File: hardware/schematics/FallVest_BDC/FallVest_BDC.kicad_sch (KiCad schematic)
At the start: 6 parts, among them U1 STP55NF06L, U2 TO-220, U3 4554

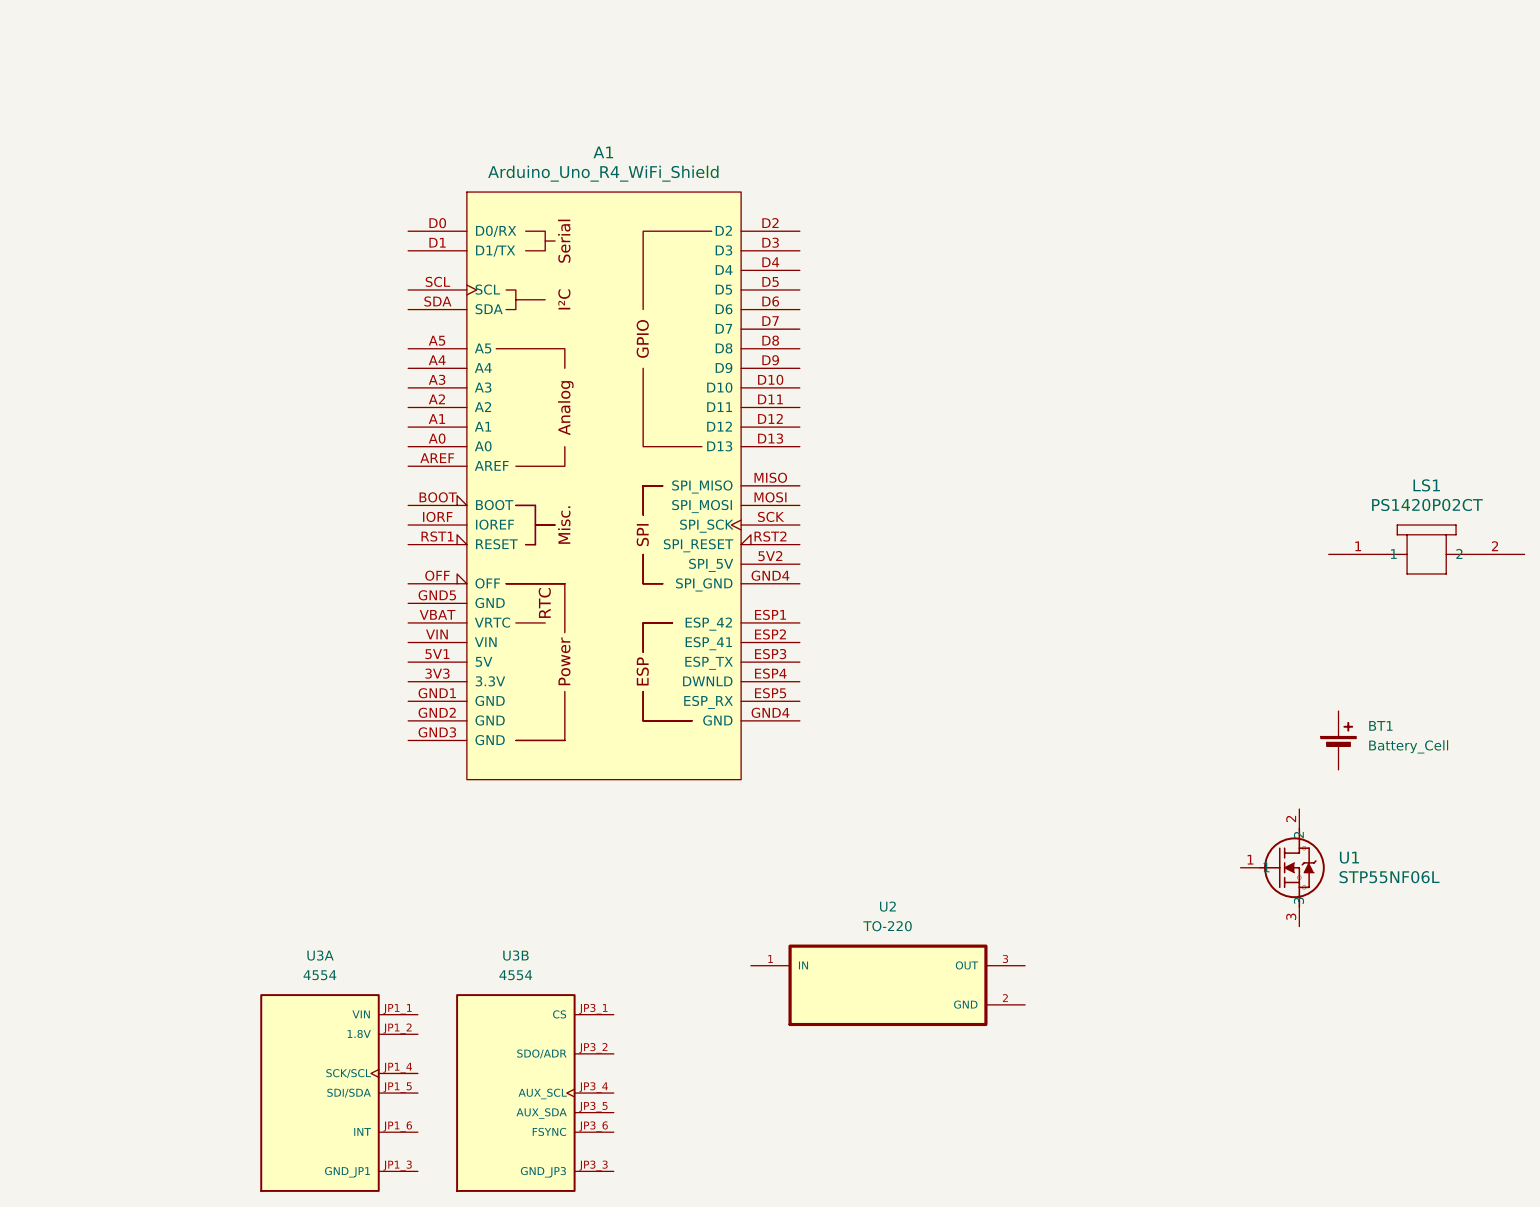
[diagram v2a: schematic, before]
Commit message: Wired most components
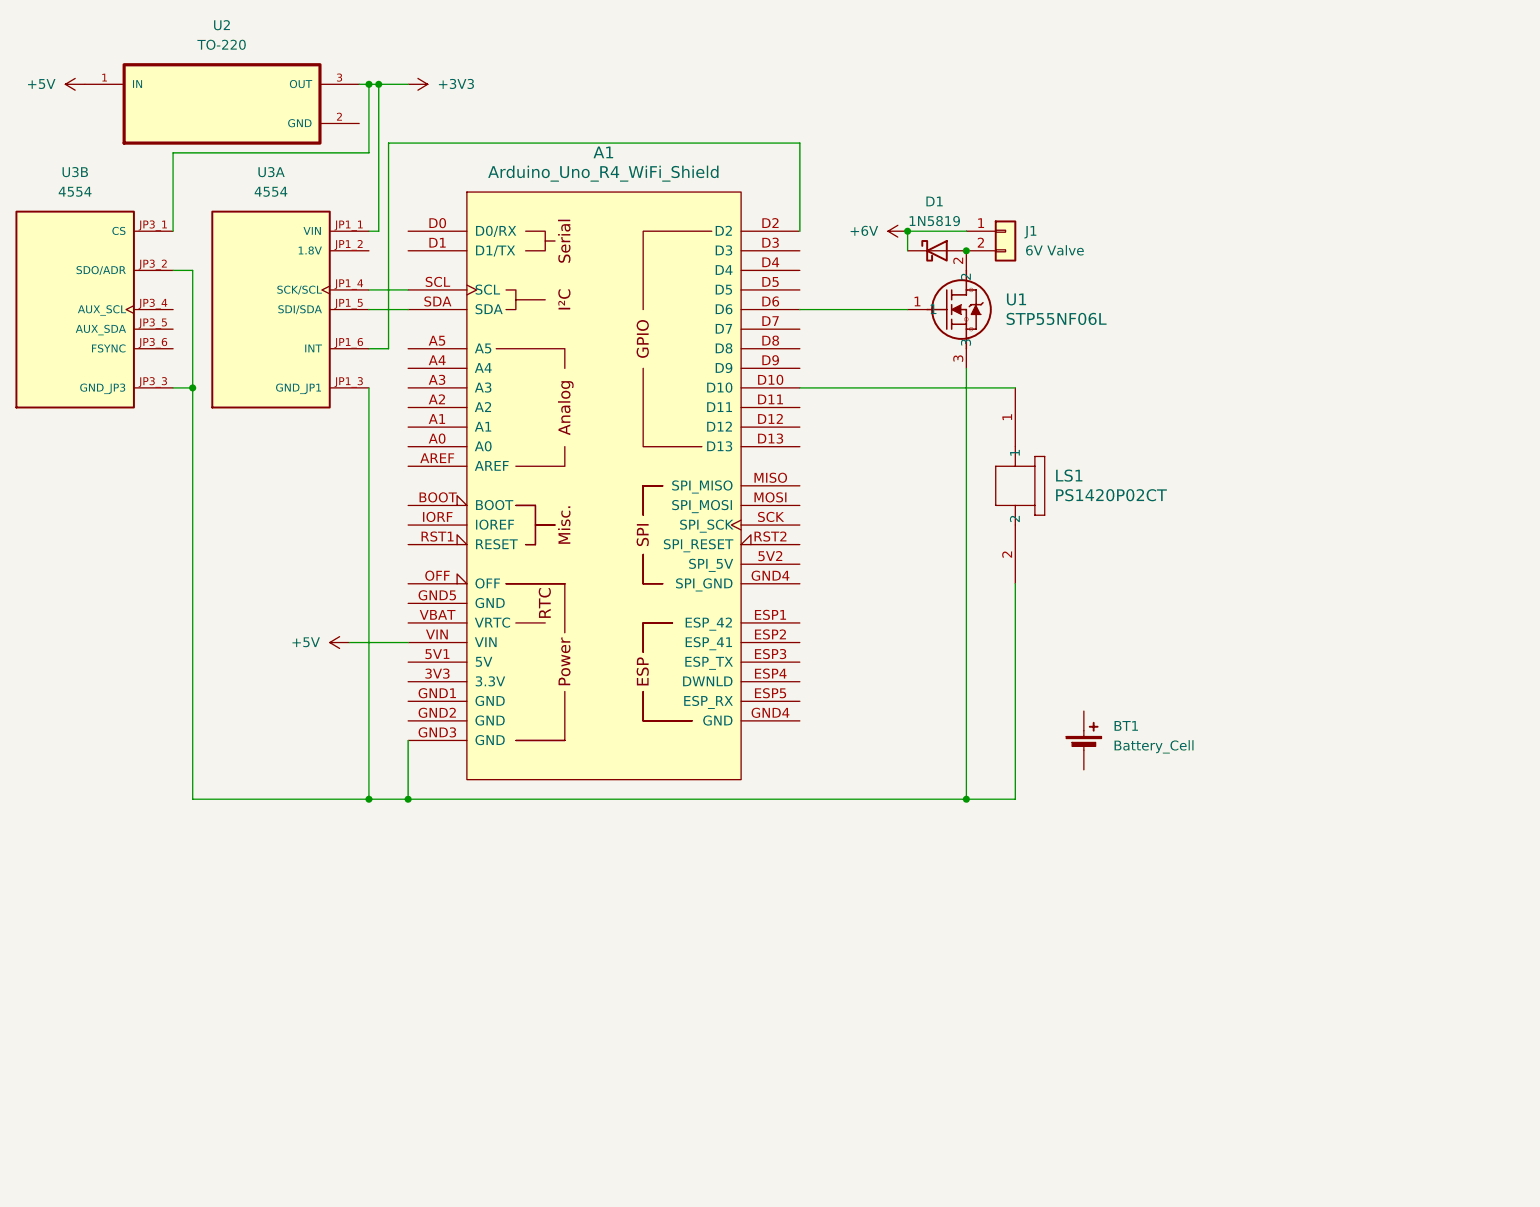
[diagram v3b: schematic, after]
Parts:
- added D1: 1N5819, Diode_THT:D_DO-41_SOD81_P10.16mm_Horizontal, symbol Diode:1N5819
- added J1: 6V Valve, symbol Connector_Generic:Conn_01x02
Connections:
- net +3V3: now reaches U3.JP3_1 (CS)
- net +3V3: now also U2.3 (OUT), U3.JP1_1 (VIN)
- net at U3.JP3_2 (SDO/ADR): now also A1.GND3 (GND), LS1.2, U1.3, U3.JP1_3 (GND_JP1), U3.JP3_3 (GND_JP3)
- net at LS1.1: now also A1.D10
- net at U3.JP1_4 (SCK/SCL): now also A1.SCL
- net at U3.JP1_5 (SDI/SDA): now also A1.SDA
- net at U3.JP1_6 (INT): now also A1.D2
- net at A1.D6: now also U1.1
- net +5V: now reaches A1.VIN
- net +5V: now also U2.1 (IN)
- net at U1.2: now also D1.2 (A), J1.2 (Pin_2)
- new net +6V: D1.1 (K), J1.1 (Pin_1)
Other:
- moved on the sheet: BT1, LS1, U1, U2, U3A, U3B

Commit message: Updated Schematic
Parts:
- removed D1: 1N5819, Diode_THT:D_DO-41_SOD81_P10.16mm_Horizontal, symbol Diode:1N5819
- removed J1: 6V Valve, symbol Connector_Generic:Conn_01x02
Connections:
- net at A1.GND3 (GND), U1.3, U3.JP1_3 (GND_JP1)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: no longer LS1.2
- net at LS1.1: now also A1.5V1 (5V); no longer A1.D10
- net at U1.2: now also LS1.2
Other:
- moved on the sheet: BT1, LS1

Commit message: Moving around and adding some stuff
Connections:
- net GND: now reaches A1.GND3 (GND), U1.3, U3.JP1_3 (GND_JP1), U3.JP3_2 (SDO/ADR), U3.JP3_3 (GND_JP3)
- net GND: now also U2.2 (GND)
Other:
- moved on the sheet: BT1, U2

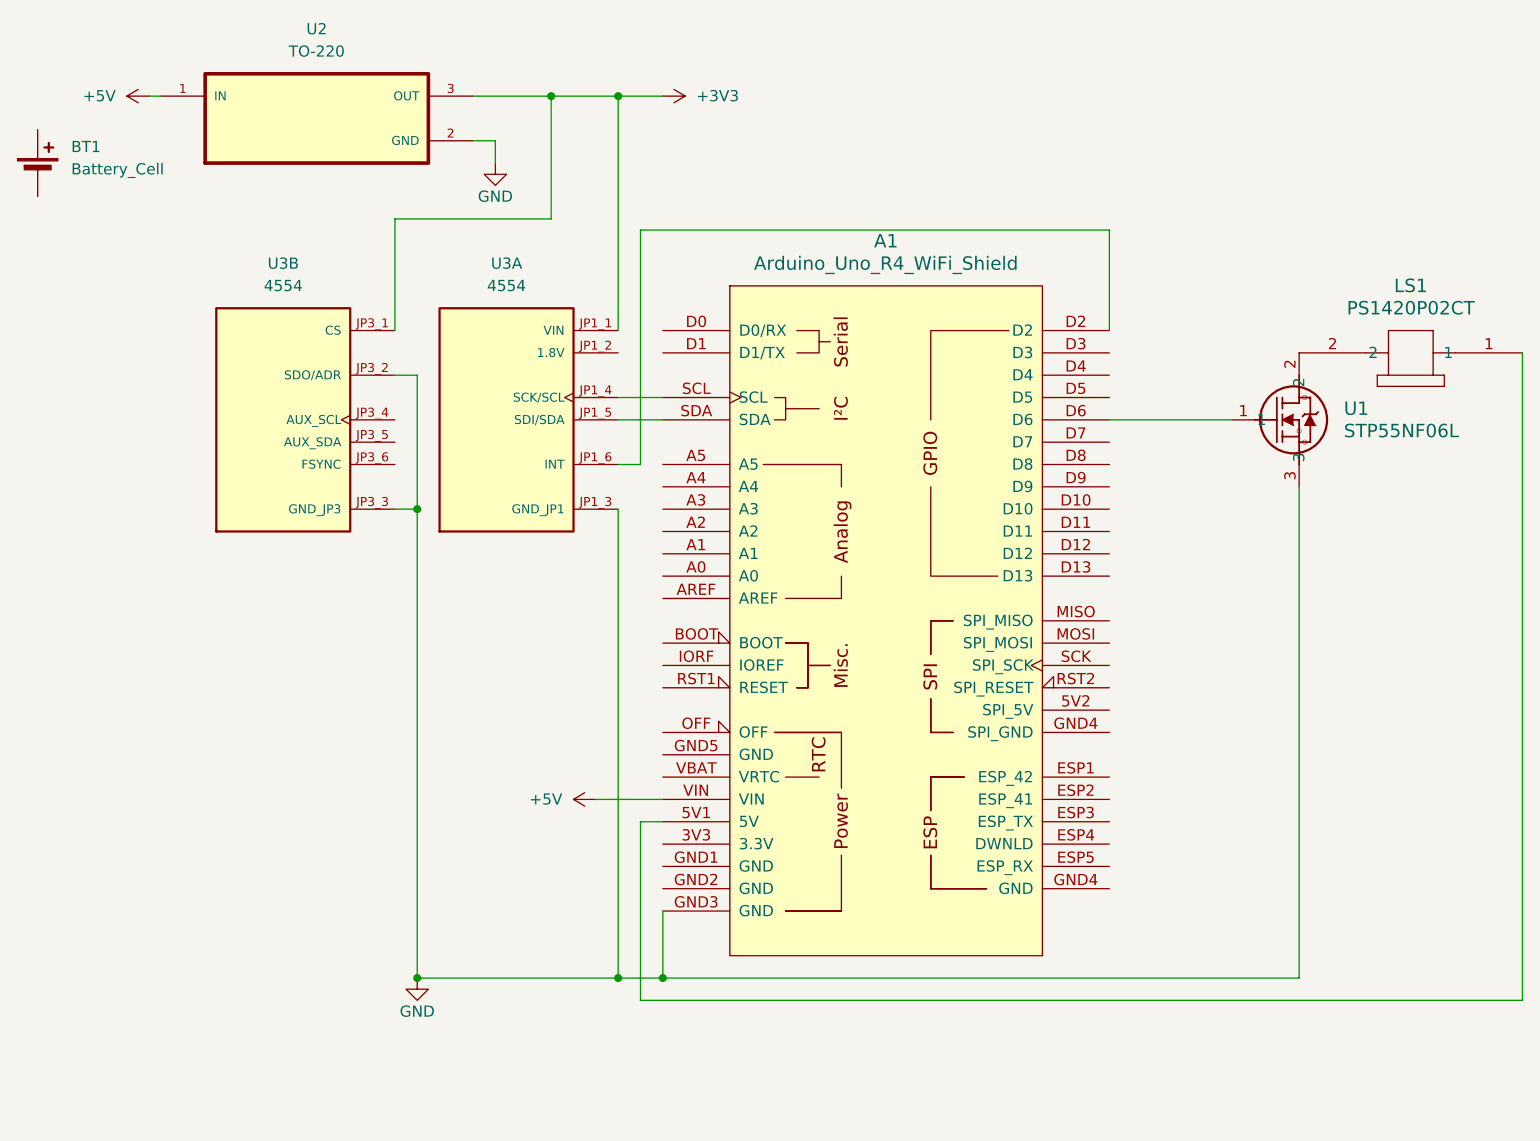
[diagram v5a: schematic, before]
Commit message: Modified
Got rid of the regulator, need to check on pinout for sensor, and where the air valve will be located in the circuit.
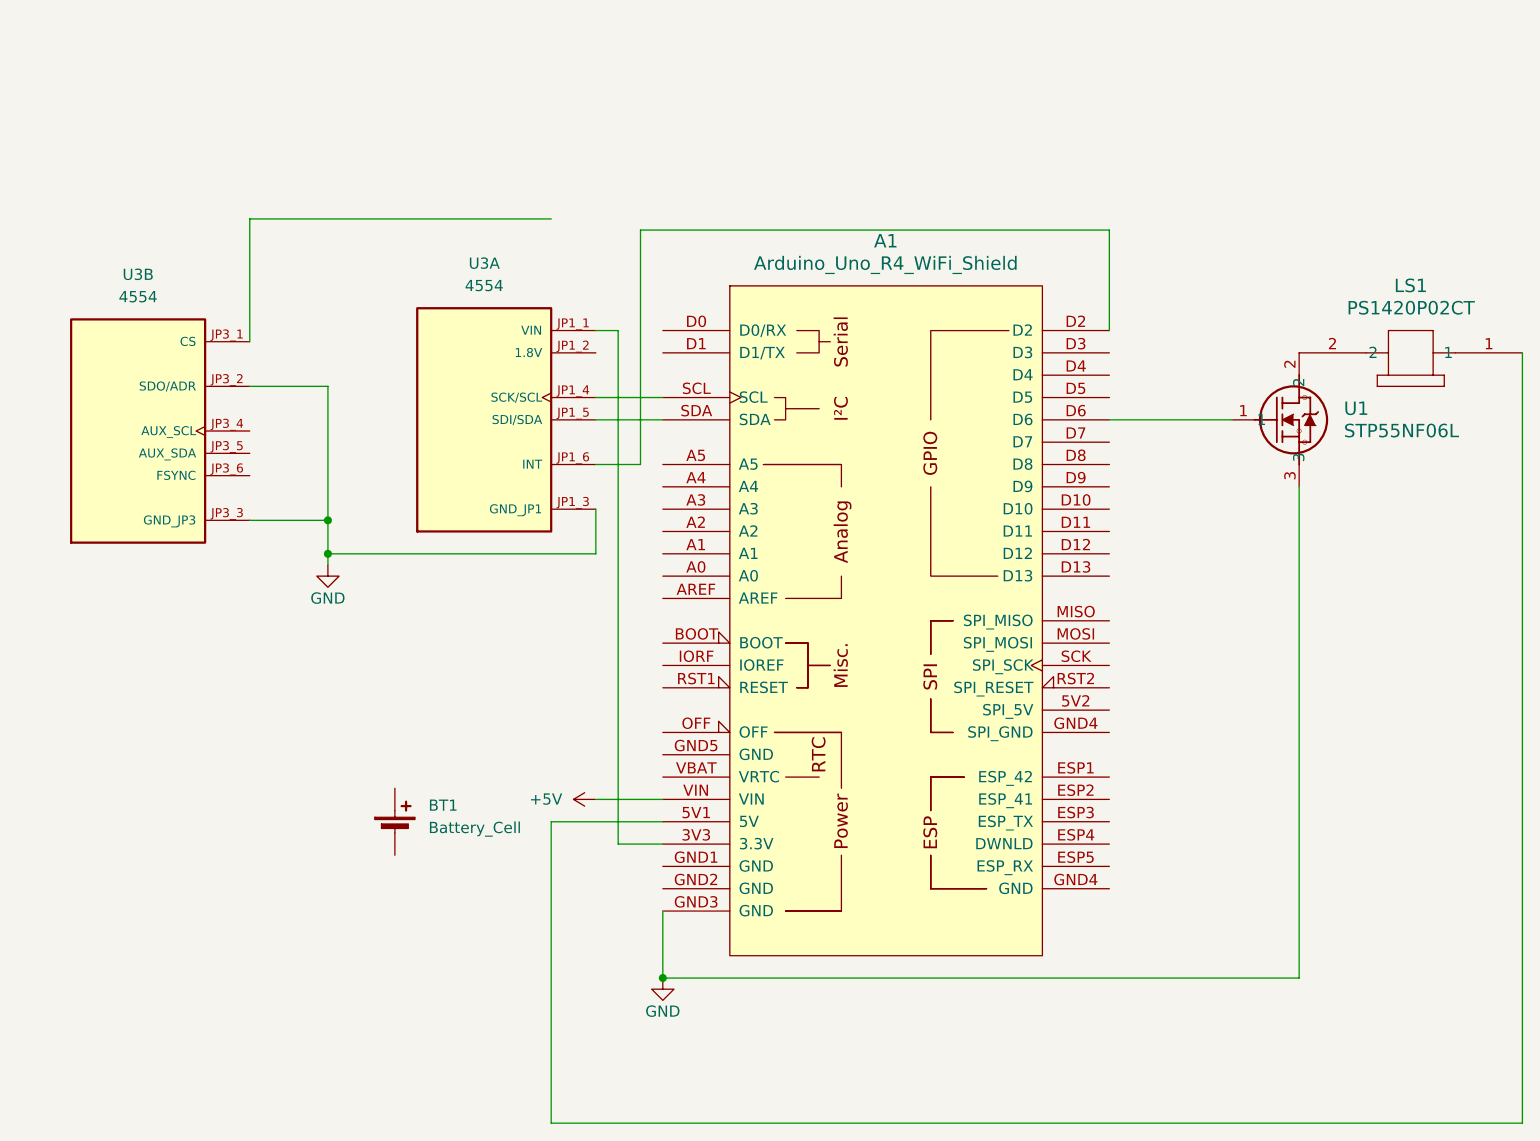
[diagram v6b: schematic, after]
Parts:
- removed U2: TO-220, LM3940IT-3.3:TO254P1054X470X1955-3, symbol EE_VEST_SYM:TO-220_3.3V-Reg
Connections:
- net at A1.3V3 (3.3V): now also U3.JP1_1 (VIN)
- net +3V3: no longer names the net of U3.JP3_1 (CS)
- net +3V3: no longer U3.JP1_1 (VIN)
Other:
- moved on the sheet: BT1, U3A, U3B
